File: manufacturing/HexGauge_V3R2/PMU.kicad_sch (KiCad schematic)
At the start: 13 parts, among them Q1 Q_PMOS_GSD, U2 TPMP2359D

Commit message: Started Board Rev3
Optimize Component Costs
Smaller Buck Converter ->
Move STM32 3mm to the right to simplify SD Card, IMU, TFT routing
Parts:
- removed C14: 22n, Capacitor_SMD:C_0402_1005Metric, symbol Device:C
- removed C15, C16: 47u, Capacitor_SMD:C_1210_3225Metric, symbol Device:C
- removed R11: 10k, Resistor_SMD:R_0402_1005Metric, symbol Device:R
- removed R8: 33k, Resistor_SMD:R_0402_1005Metric, symbol Device:R
- removed R9: 560k, Resistor_SMD:R_0603_1608Metric, symbol Device:R
- removed U2: TPMP2359D, Package_TO_SOT_SMD:TSOT-23-6, symbol Regulator_Switching:TPMP2359
- added C4: 100n, Capacitor_SMD:C_0402_1005Metric, symbol Device:C
- added C6: 10u, Capacitor_SMD:C_0805_2012Metric_Pad1.18x1.45mm_HandSolder, symbol Device:C
- added C6: 2u2, Capacitor_SMD:C_0805_2012Metric_Pad1.18x1.45mm_HandSolder, symbol Device:C
- added R18: 100k, Resistor_SMD:R_0402_1005Metric, symbol Device:R
- added U2: LMR16006YQ3, Package_TO_SOT_SMD:SOT-23-6, symbol Regulator_Switching:LMR16006YQ3
- L1: value 4u7 -> 3u3; footprint Inductor_SMD:L_Wuerth_WE-TPC-3816 -> Inductor_SMD:L_7.3x7.3_H4.5; LCSC Part # C182156 -> (none)
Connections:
- net BUCK_BST: now also C4.1, U2.1 (CB)
- net BUCK_EN: now also R18.1, U2.4 (~{SHDN})
- net BUCK_IN: now also C6.1, U2.5 (VIN)
- net BUCK_OUT: now also C4.2, U2.6 (SW)
- net GND: now also C6.2, C6.2, R18.2, U2.2 (GND)
- net +3V3 renamed +3.3V
- net +3.3V: now also C6.1, U2.3 (FB)
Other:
- note removed: "33k||560k=31k16"
- note removed: "Vout = 3V3 R1 = 31k25 R2 = 10k L1 = 3u3 Cin = 47u Cout = 47u"
- moved on the sheet: L1

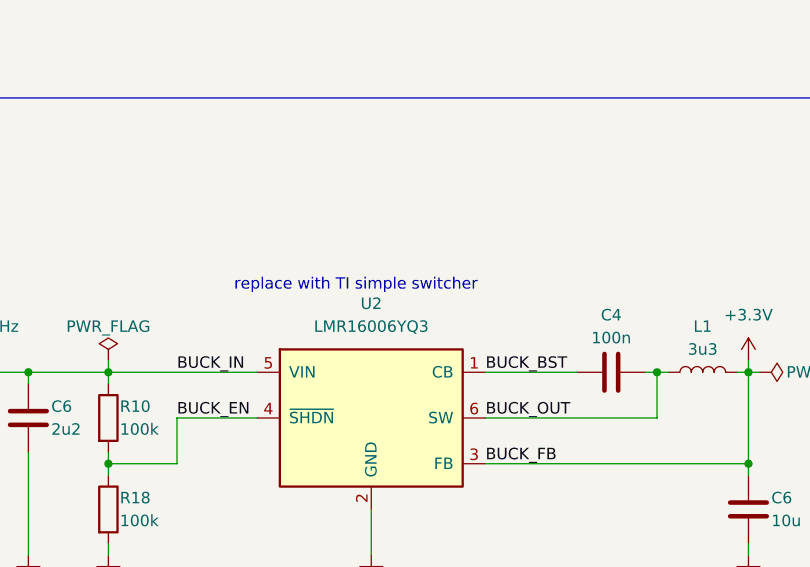
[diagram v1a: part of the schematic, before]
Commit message: added Datasheets to components
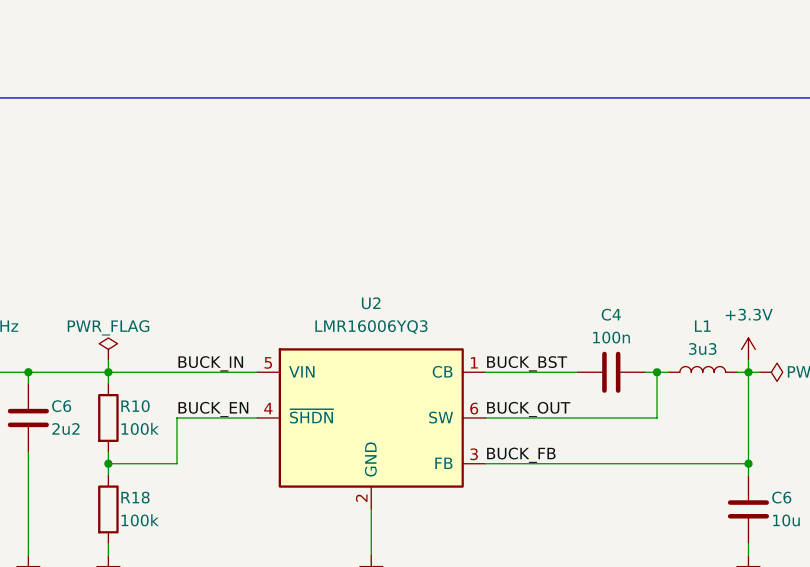
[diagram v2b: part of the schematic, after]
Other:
- note removed: "replace with TI simple switcher"
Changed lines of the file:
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@@
-    (effects (font (size 1.27 1.27)) (justify left bottom))
-  )
-  (text "replace with TI simple switcher" (at 101.6 72.39 0)
     (effects (font (size 1.27 1.27)) (justify left bottom))
   )
@@
       (effects (font (size 1.27 1.27) italic) hide)
     )
-    (property "Datasheet" "http://www.ti.com/lit/ds/symlink/lmr16006y-q1.pdf" (at 106.68 74.93 0)
+    (property "Datasheet" "https://www.ti.com/lit/ds/symlink/lmr50410-q1.pdf?HQS=dis-mous-null-mousermode-dsf-pf-null-wwe&ts=1691439607164&ref_url=https%253A%252F%252Fnl.mouser.com%252F" (at 106.68 74.93 0)
       (effects (font (size 1.27 1.27)) hide)
     )

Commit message: FInalised Revision 2 Design
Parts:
- C6: LCSC Part # C96446 -> (none)
- C6: LCSC Part # C23630 -> (none)
- F1: footprint Inductor_SMD:L_0805_2012Metric -> Inductor_SMD:L_1206_3216Metric
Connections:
- net +3.3V renamed +3V3
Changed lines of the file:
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@@
+    )
+  )
+  (symbol (lib_id "power:+3V3") (at 158.75 80.01 0) (unit 1)
+    (in_bom yes) (on_board yes) (dnp no) (fields_autoplaced)
+    (property "Reference" "#PWR020" (at 158.75 83.82 0)
+      (effects (font (size 1.27 1.27)) hide)
+    )
+    (property "Value" "+3V3" (at 158.75 74.93 0)
+      (effects (font (size 1.27 1.27)))
+    )
+    (property "Footprint" "" (at 158.75 80.01 0)
+      (effects (font (size 1.27 1.27)) hide)
+    )
+    (property "Datasheet" "" (at 158.75 80.01 0)
+      (effects (font (size 1.27 1.27)) hide)
+    )
+    (pin "1")
+    (instances
+      (project "STM32F4_HexGauge_V3"
+        (path "/1671c3d2-535f-4cd5-a65b-02e5c9ad18e5/166e52e6-ad52-4e82-85bb-6068cde833c9"
+          (reference "#PWR020") (unit 1)
+        )
+      )
     )
   )
@@
       (effects (font (size 1.27 1.27)) hide)
     )
-    (property "LCSC Part #" "C96446" (at 158.75 96.52 0)
+    (property "LCSC Part #" "" (at 158.75 96.52 0)
       (effects (font (size 1.27 1.27)) hide)
     )
@@
       (effects (font (size 1.27 1.27)))
     )
-    (property "Footprint" "Inductor_SMD:L_0805_2012Metric" (at 64.77 80.01 0)
+    (property "Footprint" "Inductor_SMD:L_1206_3216Metric" (at 64.77 80.01 0)
       (effects (font (size 1.27 1.27)) (justify left) hide)
     )
@@
       (effects (font (size 1.27 1.27)) hide)
     )
-    (property "LCSC Part #" "C23630" (at 78.74 86.36 0)
+    (property "LCSC Part #" "" (at 78.74 86.36 0)
       (effects (font (size 1.27 1.27)) hide)
     )
@@
         )
       )
-    )
-  )
-  (symbol (lib_id "power:+3.3V") (at 158.75 80.01 0) (unit 1)
-    (in_bom yes) (on_board yes) (dnp no) (fields_autoplaced)
-    (property "Reference" "#PWR020" (at 158.75 83.82 0)
-      (effects (font (size 1.27 1.27)) hide)
-    )
-    (property "Value" "+3.3V" (at 158.75 74.93 0)
-      (effects (font (size 1.27 1.27)))
-    )
-    (property "Footprint" "" (at 158.75 80.01 0)
-      (effects (font (size 1.27 1.27)) hide)
-    )
-    (property "Datasheet" "" (at 158.75 80.01 0)
-      (effects (font (size 1.27 1.27)) hide)
-    )
-    (pin "1")
-    (instances
-      (project "STM32F4_HexGauge_V3"
-        (path "/1671c3d2-535f-4cd5-a65b-02e5c9ad18e5/166e52e6-ad52-4e82-85bb-6068cde833c9"
-          (reference "#PWR020") (unit 1)
-        )
-      )

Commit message: upd fields
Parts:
- C4, D2, FB1, Q1, R10, R18: Dist (none) -> LCSC
- C6: Dist (none) -> Self
- F1: Dist (none) -> Mouser; LCSC Part # C209741 -> (none)
- L1, U2: Dist (none) -> Mouser
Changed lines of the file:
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@@
+      (effects (font (size 1.27 1.27)) hide)
+    )
+    (property "Dist" "Mouser" (at 116.84 86.36 0)
       (effects (font (size 1.27 1.27)) hide)
     )
@@
       (effects (font (size 1.27 1.27)) hide)
     )
+    (property "Dist" "Self" (at 158.75 96.52 0)
+      (effects (font (size 1.27 1.27)) hide)
+    )
     (pin "1")
     (pin "2")
@@
       (effects (font (size 1.27 1.27)) hide)
     )
+    (property "Dist" "LCSC" (at 71.12 81.28 0)
+      (effects (font (size 1.27 1.27)) hide)
+    )
     (pin "1")
     (pin "2")
@@
     )
     (property "LCSC Part #" "C1525" (at 143.51 81.28 0)
+      (effects (font (size 1.27 1.27)) hide)
+    )
+    (property "Dist" "LCSC" (at 143.51 81.28 0)
       (effects (font (size 1.27 1.27)) hide)
     )
@@
     )
     (property "LCSC Part #" "C8598" (at 53.34 71.12 0)
+      (effects (font (size 1.27 1.27)) hide)
+    )
+    (property "Dist" "LCSC" (at 53.34 71.12 0)
       (effects (font (size 1.27 1.27)) hide)
     )
@@
       (effects (font (size 1.27 1.27)) hide)
     )
-    (property "LCSC Part #" "C209741" (at 59.69 81.28 0)
+    (property "LCSC Part #" "" (at 59.69 81.28 0)
+      (effects (font (size 1.27 1.27)) hide)
+    )
+    (property "Dist" "Mouser" (at 59.69 81.28 0)
       (effects (font (size 1.27 1.27)) hide)
     )
@@
       (effects (font (size 1.27 1.27)) hide)
     )
+    (property "Dist" "Mouser" (at 153.67 81.28 0)
+      (effects (font (size 1.27 1.27)) hide)
+    )
     (pin "1")
     (pin "2")
@@
       (effects (font (size 1.27 1.27)) hide)
     )
+    (property "Dist" "LCSC" (at 87.63 86.36 0)
+      (effects (font (size 1.27 1.27)) hide)
+    )
     (pin "1")
     (pin "2")
@@
     )
     (property "LCSC Part #" "" (at 78.74 86.36 0)
+      (effects (font (size 1.27 1.27)) hide)
+    )
+    (property "Dist" "Self" (at 78.74 86.36 0)
       (effects (font (size 1.27 1.27)) hide)
     )
@@
       (effects (font (size 1.27 1.27)) hide)
     )
+    (property "Dist" "LCSC" (at 45.72 83.82 0)
+      (effects (font (size 1.27 1.27)) hide)
+    )
     (pin "1")
     (pin "2")
@@
       (effects (font (size 1.27 1.27)) hide)
     )
+    (property "Dist" "LCSC" (at 87.63 96.52 0)
+      (effects (font (size 1.27 1.27)) hide)
+    )
